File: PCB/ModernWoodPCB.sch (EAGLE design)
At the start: 231 parts, among them Q1 FS8205A, U1 ESP32-S3HOLE, U2 ME6211C33M5G

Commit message: Revision 2 of PCB and Finished
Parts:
- removed Q1: FS8205A, FS8205A:FS8205A
- added Q2: FS8205, FS8205:FS8205
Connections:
- removed net DWOC: Q1.G2, U$96.OC
- removed net DWOD: Q1.G1, U$96.OD
- new net N$31: Q2.G1, U$96.OD
- new net N$32: Q2.G2, U$96.OC
- net B-: now also Q2.S1; no longer Q1.S1
- net GND: now also Q2.S2; no longer Q1.S2
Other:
- note added: "3"
- note removed: "1"
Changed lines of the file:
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@@
 <part name="U$95" library="TP4056" deviceset="TP4056" device=""/>
 <part name="U$96" library="DW01A" deviceset="DW01A" device=""/>
-<part name="Q1" library="FS8205A" deviceset="FS8205A" device=""/>
 <part name="BATTERY" library="con-headers-jp" deviceset="F-1X02-" device="SIP-100-40"/>
 <part name="GND1" library="supply1" library_urn="urn:adsk.eagle:library:371" deviceset="GND" device=""/>
@@
 <part name="P+17" library="supply1" library_urn="urn:adsk.eagle:library:371" deviceset="VCC" device=""/>
 <part name="FRAME1" library="frames" library_urn="urn:adsk.eagle:library:229" deviceset="FRAME_D_L" device=""/>
+<part name="Q2" library="FS8205" deviceset="FS8205" device=""/>
 </parts>
 <sheets>
@@
 <plain>
 <text x="655.42" y="45.02" size="3.81" layer="94">ModernWood</text>
-<text x="734.42" y="34.02" size="3.81" layer="94">1</text>
+<text x="734.42" y="34.02" size="3.81" layer="94">3</text>
 <text x="686.42" y="36.02" size="3.81" layer="94">Document 1</text>
 <text x="645.42" y="55.02" size="3.81" layer="94">By Carlos Lopez Martinez</text>
@@
 </instance>
 <instance part="U$96" gate="G$1" x="680.6" y="279.76" smashed="yes"/>
-<instance part="Q1" gate="G$1" x="688.22" y="239.12" smashed="yes" rot="R270">
-<attribute name="VALUE" x="675.52" y="250.55" size="1.778" layer="96" rot="R270"/>
-<attribute name="NAME" x="695.84" y="250.55" size="1.778" layer="95" rot="R270"/>
-</instance>
 <instance part="BATTERY" gate="G$1" x="619.64" y="239.12" smashed="yes" rot="R180">
 <attribute name="NAME" x="620.91" y="235.818" size="1.778" layer="95" rot="R180"/>
@@
 <attribute name="SHEET" x="727.7" y="29.29" size="2.54" layer="94"/>
 </instance>
+<instance part="Q2" gate="G$1" x="682.22" y="246.51" smashed="yes" rot="R270">
+<attribute name="NAME" x="684.506" y="243.97" size="1.778" layer="95" rot="R270" align="top-left"/>
+<attribute name="VALUE" x="680.188" y="243.97" size="1.778" layer="96" rot="R270"/>
+</instance>
 </instances>
 <busses>
@@
 <segment>
 <pinref part="GND6" gate="1" pin="GND"/>
-<wire x1="700.92" y1="256.9" x2="700.92" y2="239.12" width="0.1524" layer="91"/>
-<pinref part="Q1" gate="G$1" pin="S2"/>
-<wire x1="700.92" y1="239.12" x2="700.92" y2="231.5" width="0.1524" layer="91"/>
-<wire x1="698.38" y1="239.12" x2="700.92" y2="239.12" width="0.1524" layer="91"/>
-<junction x="700.92" y="239.12"/>
+<wire x1="700.92" y1="256.9" x2="700.92" y2="231.5" width="0.1524" layer="91"/>
 <pinref part="R3" gate="G$1" pin="2"/>
+<pinref part="Q2" gate="G$1" pin="S2"/>
+<wire x1="692.38" y1="246.51" x2="700.92" y2="246.51" width="0.1524" layer="91"/>
+<wire x1="700.92" y1="246.51" x2="700.92" y2="256.9" width="0.1524" layer="91"/>
+<junction x="700.92" y="256.9"/>
 </segment>
 <segment>
@@
 <pinref part="U$96" gate="G$1" pin="GND"/>
 <wire x1="670.44" y1="274.68" x2="660.28" y2="274.68" width="0.1524" layer="91"/>
-<pinref part="Q1" gate="G$1" pin="S1"/>
-<wire x1="678.06" y1="239.12" x2="660.28" y2="239.12" width="0.1524" layer="91"/>
 <wire x1="660.28" y1="239.12" x2="660.28" y2="274.68" width="0.1524" layer="91"/>
 <wire x1="660.28" y1="239.12" x2="652.66" y2="239.12" width="0.1524" layer="91"/>
-<junction x="660.28" y="239.12"/>
 <label x="652.66" y="239.12" size="1.778" layer="95"/>
 <pinref part="C2" gate="G$1" pin="2"/>
 <junction x="660.28" y="274.68"/>
+<pinref part="Q2" gate="G$1" pin="S1"/>
+<wire x1="660.28" y1="274.68" x2="660.28" y2="246.51" width="0.1524" layer="91"/>
+<wire x1="660.28" y1="246.51" x2="672.06" y2="246.51" width="0.1524" layer="91"/>
 </segment>
 </net>
@@
 </segment>
 </net>
-<net name="DWOD" class="0">
-<segment>
-<pinref part="Q1" gate="G$1" pin="G1"/>
-<pinref part="U$96" gate="G$1" pin="OD"/>
-<wire x1="680.6" y1="244.2" x2="680.6" y2="261.98" width="0.1524" layer="91"/>
-<wire x1="680.6" y1="261.98" x2="685.68" y2="261.98" width="0.1524" layer="91"/>
-<label x="680.6" y="254.36" size="1.778" layer="95"/>
-</segment>
-</net>
-<net name="DWOC" class="0">
-<segment>
-<pinref part="Q1" gate="G$1" pin="G2"/>
-<pinref part="U$96" gate="G$1" pin="OC"/>
-<wire x1="690.76" y1="244.2" x2="690.76" y2="261.98" width="0.1524" layer="91"/>
-<label x="690.76" y="254.36" size="1.778" layer="95"/>
-</segment>
-</net>
 <net name="DWVCC" class="0">
 <segment>
@@
 </segment>
 </net>
+<net name="N$31" class="0">
+<segment>
+<pinref part="Q2" gate="G$1" pin="G1"/>
+<pinref part="U$96" gate="G$1" pin="OD"/>
+<wire x1="677.14" y1="251.59" x2="677.14" y2="261.98" width="0.1524" layer="91"/>
+<wire x1="677.14" y1="261.98" x2="685.68" y2="261.98" width="0.1524" layer="91"/>
+</segment>
+</net>
+<net name="N$32" class="0">
+<segment>
+<pinref part="U$96" gate="G$1" pin="OC"/>
+<pinref part="Q2" gate="G$1" pin="G2"/>
+<wire x1="690.76" y1="261.98" x2="690.76" y2="251.59" width="0.1524" layer="91"/>
+<wire x1="690.76" y1="251.59" x2="687.3" y2="251.59" width="0.1524" layer="91"/>
+</segment>
+</net>

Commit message: Fixed 5V on Tp4056 status pins
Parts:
- added R10, R8: 1M, resistors:1K
- added R11, R9: 2M, resistors:1K
- R6: value 8200000 -> 4M
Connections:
- new net CHRG_3: R8.2, R9.1, U1.IO2
- new net STDBY_3: R10.2, R11.1, U1.IO21
- net CHRG: now also R8.1; no longer U1.IO2
- net GND: now also R11.2, R9.2
- net STDBY: now also R10.1; no longer U1.IO21
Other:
- note added: "5"
- note removed: "3"
- moved on the sheet: BOOT, FN_KEY, R4, R7, SCREEN, U1

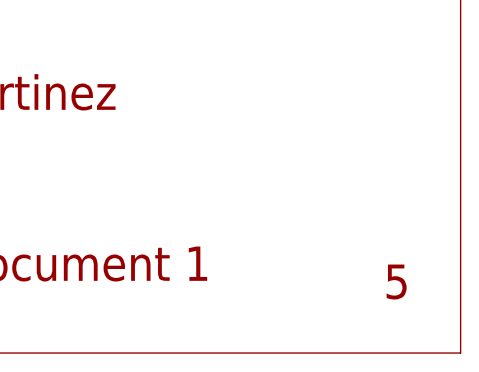
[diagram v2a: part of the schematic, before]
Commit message: Fixed value texts for smd resistors
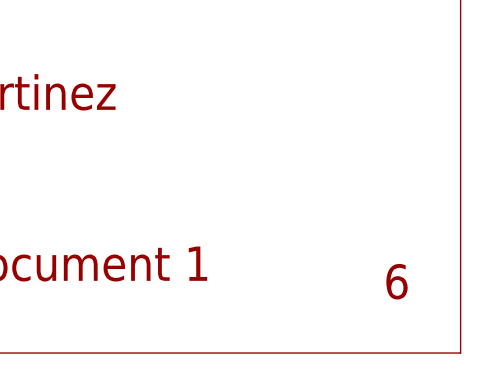
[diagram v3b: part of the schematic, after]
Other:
- note added: "6"
- note removed: "5"
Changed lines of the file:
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@@
 <plain>
 <text x="693.52" y="45.02" size="3.81" layer="94">ModernWood</text>
-<text x="772.52" y="34.02" size="3.81" layer="94">5</text>
+<text x="772.52" y="34.02" size="3.81" layer="94">6</text>
 <text x="724.52" y="36.02" size="3.81" layer="94">Document 1</text>
 <text x="683.52" y="55.02" size="3.81" layer="94">By Carlos Lopez Martinez</text>
